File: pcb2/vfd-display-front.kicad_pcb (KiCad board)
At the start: 2 copper layers, 201.9 x 54.6 mm, 61 parts, among them CON1 AVR-ISP-10, IC1 ATMEGA88A-A, IC2 TD62C950RF, IC3 TD62C950RF, J1 HEADER_5, P1 CONN_02X05, P2 CONN_01X03, P3 CONN_01X02, P4 CONN_01X04, P5 CONN_01X02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

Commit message: Update.
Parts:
- moved CON1 0.76 mm to (116.3, 39.9)
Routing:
- net /MOSI: track 0.00 -> 41.0 mm
- net /MISO: track 0.00 -> 23.7 mm
- net /SCK: track 0.00 -> 20.1 mm
- net /SCL: track 17.9 -> 0.00 mm
- net /SDA: track 17.3 -> 0.00 mm

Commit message: Board almost done.
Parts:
- moved R13 35.2 mm to (101.1, 33.0), turned to 270 degrees
- moved Q1 35.1 mm to (101.6, 27.4)
- moved C12 25.9 mm to (178.8, 43.4), turned to 270 degrees
- moved C19 25.2 mm to (66.3, 29.0)
- moved U3 24.9 mm to (76.7, 29.5), turned to 270 degrees
- moved P6 23.7 mm to (84.6, 30.0)
- moved R14 21.4 mm to (104.9, 31.2), turned to 270 degrees
- moved C17 17.8 mm to (93.5, 29.2), turned to 180 degrees
- moved R9 16.4 mm to (56.4, 36.1), turned to 270 degrees
- moved P5 15.0 mm to (47.0, 40.9), turned to 0 degrees
- moved R8 14.1 mm to (59.4, 36.1), turned to 270 degrees
- moved C10 2.84 mm to (96.8, 47.8), turned to 180 degrees
- moved C15 2.70 mm to (51.1, 39.6), turned to 90 degrees
- moved C14 1.52 mm to (184.4, 45.2)
- moved P3 1.30 mm to (56.1, 49.5)
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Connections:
- IC1 pad 10: Net-(IC1-Pad10) -> /CHG
- IC1 pad 11: Net-(IC1-Pad11) -> /CK
- IC1 pad 12: Net-(IC1-Pad12) -> /S-IN
- IC1 pad 13: Net-(IC1-Pad13) -> /STB
- IC1 pad 14: Net-(IC1-Pad14) -> /CL
- IC1 pad 9: Net-(IC1-Pad9) -> /SPKR
- U2 pad 6: Net-(U2-Pad6) -> /BTN_WAKE
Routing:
- net +5V: track 23.4 -> 245.3 mm, vias 0 -> 4
- net /OVF: track 0.00 -> 146.0 mm, vias 0 -> 4
- net /CL: track 0.00 -> 142.6 mm, vias 0 -> 2
- net /STB: track 0.00 -> 140.7 mm, vias 0 -> 2
- net /CK: track 0.00 -> 119.5 mm, vias 0 -> 6
- net /CHG: track 0.00 -> 112.8 mm, vias 0 -> 6
- net /SDA: track 0.00 -> 110.0 mm, vias 0 -> 6
- net /SCL: track 0.00 -> 105.8 mm, vias 0 -> 2
- net /S-IN: track 0.00 -> 79.5 mm
- net GND: track 20.6 -> 93.6 mm
- net +3V3: track 0.00 -> 71.3 mm
- net Net-(P3-Pad1): track 0.00 -> 22.7 mm
- net Net-(Q1-Pad1): track 0.00 -> 19.2 mm
- net Net-(P1-Pad5): track 0.00 -> 17.4 mm
- net Net-(P1-Pad3): track 0.00 -> 17.2 mm
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
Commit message: Board beta complete.
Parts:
- moved R13 6.18 mm to (95.0, 34.0), turned to 0 degrees
- moved C10 5.08 mm to (101.9, 47.8), turned to 90 degrees
- moved C13 4.06 mm to (116.3, 29.0)
- moved C11 3.97 mm to (122.9, 29.5)
- moved C12 2.62 mm to (177.5, 41.1)
- moved C19 2.59 mm to (65.8, 31.5)
- moved L1 2.54 mm to (132.1, 30.5)
- moved C7 2.29 mm to (134.1, 53.6)
- moved C17 1.78 mm to (93.5, 27.4)
- moved P3 1.52 mm to (56.1, 48.0)
- moved P6 1.48 mm to (85.3, 28.7)
- moved U3 1.48 mm to (78.0, 28.7)
- moved R14 1.37 mm to (105.4, 30.0)
- moved R1 0.92 mm to (121.2, 38.6)
- moved C8 0.25 mm to (67.3, 45.2)
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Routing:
- net GND: track 93.6 -> 193.8 mm, vias 0 -> 4
- net /SPKR: track 0.00 -> 49.5 mm, vias 0 -> 2
- net +5V: track 245.3 -> 280.9 mm, vias 4 -> 6
- net +48V: track 154.3 -> 149.4 mm
- net Net-(C3-Pad1): track 47.0 -> 50.4 mm
- net /CK: track 119.5 -> 122.7 mm
- net /CHG: track 112.8 -> 110.0 mm
- net Net-(D7-Pad2): track 21.0 -> 18.5 mm
- net Net-(C9-Pad1): track 16.1 -> 18.4 mm
- net Net-(P2-Pad1): track 8.99 -> 11.2 mm
- net Net-(C7-Pad1): track 14.4 -> 16.5 mm
- net Net-(C3-Pad2): track 52.0 -> 54.1 mm
- net +3V3: track 71.3 -> 73.4 mm
- net Net-(Q1-Pad1): track 19.2 -> 17.4 mm
- net /SCL: track 105.8 -> 107.5 mm
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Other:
- net class Default: clearance 0.2 -> 0.3; trace_width 0.25 -> 0.4; via_dia 0.6 -> 1.2; via_drill 0.4 -> 0.8
- rule trace_clearance: 0.2 -> 0.3
- rule trace_min: 0.2 -> 0.4
- rule via_min_size: 0.4 -> 0.8
- board text added: "2016"
- board text added: "DK"
- board text added: "Michał"
- board text added: "SQ2OMC"
- board text added: "Słomkowski"
- board text added: "VFD DISP"

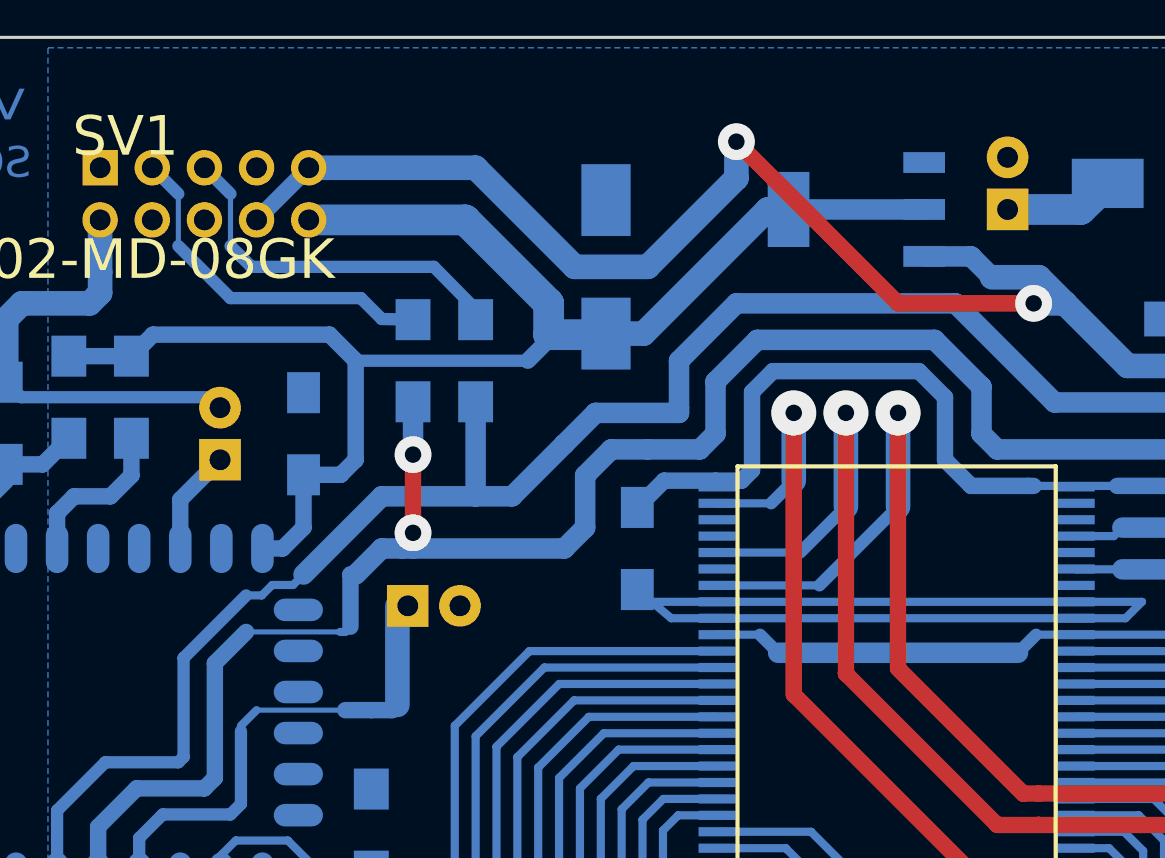
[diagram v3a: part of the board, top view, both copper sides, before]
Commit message: Make some lines thicker.
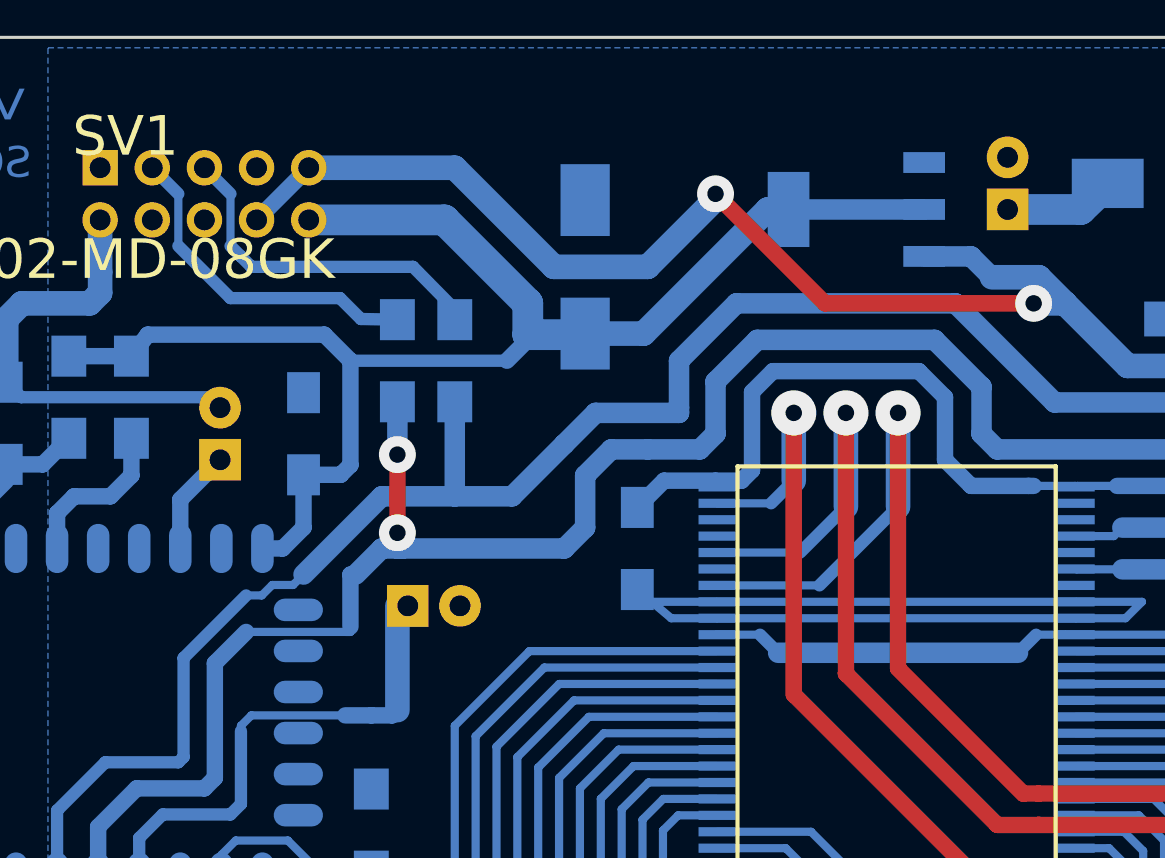
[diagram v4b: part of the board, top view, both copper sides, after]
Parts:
- moved C19 1.02 mm to (64.8, 31.5)
- moved R8 1.02 mm to (58.4, 36.1)
- moved R9 0.76 mm to (55.6, 36.1)
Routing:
- net +5V: track 280.9 -> 277.9 mm
- net +3V3: track 73.4 -> 72.3 mm
- net /SDA: track 110.2 -> 111.2 mm
- net Net-(P1-Pad5): track 17.6 -> 16.5 mm
- net Net-(P1-Pad3): track 17.2 -> 16.5 mm
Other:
- net class Default: clearance 0.3 -> 0.1
- rule pad_to_mask_clearance: 0.2 -> 0.1
- rule trace_clearance: 0.3 -> 0.1

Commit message: Add correct footprint for PCB. Fix PCB.
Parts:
- IC2, IC3: footprint futaba-vfd:futaba-vfd-SSOP60-P-0.65 -> TD62C950RF:SSOP60-P-0.65A
- R4: value 10k -> 4k7
- R5: value 10k -> 1k5
- moved C10 38.2 mm to (63.8, 50.5)
- moved C14 4.99 mm to (183.1, 50.0), turned to 90 degrees
- moved C8 4.64 mm to (68.1, 49.8)
- moved C12 4.60 mm to (177.0, 45.7), turned to 0 degrees
- moved R11 3.34 mm to (53.8, 55.6), turned to 270 degrees
- moved R3 3.10 mm to (186.9, 50.0), turned to 270 degrees
- moved IC2 2.74 mm to (166.1, 57.1)
- moved IC3 2.65 mm to (79.5, 57.1)
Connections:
- CON1 pad 3: Net-(CON1-Pad3) -> (no net)
- IC1 pad 19: Net-(IC1-Pad19) -> (no net)
- IC1 pad 2: Net-(IC1-Pad2) -> (no net)
- IC1 pad 20: Net-(IC1-Pad20) -> (no net)
- IC1 pad 22: Net-(IC1-Pad22) -> (no net)
- IC1 pad 23: Net-(IC1-Pad23) -> (no net)
- IC1 pad 24: Net-(IC1-Pad24) -> (no net)
- IC1 pad 25: Net-(IC1-Pad25) -> (no net)
- IC1 pad 26: Net-(IC1-Pad26) -> (no net)
- IC1 pad 30: Net-(IC1-Pad30) -> (no net)
- IC2 pad 1: /G34 -> (no net)
- IC2 pad 10: /G31 -> /A26
- IC2 pad 11: /G30 -> /A27
- IC2 pad 12: /G29 -> /A28
- IC2 pad 13: /G28 -> /A29
- IC2 pad 14: /G27 -> /A30
- IC2 pad 15: /G26 -> /A31
- IC2 pad 16: /G25 -> /A32
- IC2 pad 17: /G24 -> /A33
- IC2 pad 18: /G23 -> /A34
- IC2 pad 19: /G22 -> /A35
- IC2 pad 2: /G35 -> (no net)
- IC2 pad 20: /G21 -> /A36
- IC2 pad 24: /CL -> (no net)
- IC2 pad 25: (no net) -> /CHG
- IC2 pad 26: /STB -> (no net)
- IC2 pad 27: (no net) -> /CK
- IC2 pad 29: /S-IN -> /OVF
- IC2 pad 3: /G36 -> /A25
- IC2 pad 32: /OVF -> /S-IN
- IC2 pad 34: /CK -> (no net)
- IC2 pad 35: (no net) -> /STB
- IC2 pad 36: /CHG -> (no net)
- IC2 pad 37: (no net) -> /CL
- IC2 pad 4: /G37 -> /A24
- IC2 pad 41: /A36 -> /G21
- IC2 pad 42: /A35 -> /G22
- IC2 pad 43: /A34 -> /G23
- IC2 pad 44: /A33 -> /G24
- IC2 pad 45: /A32 -> /G25
- IC2 pad 46: /A31 -> /G26
- IC2 pad 47: /A30 -> /G27
- IC2 pad 48: /A29 -> /G28
- IC2 pad 49: /A28 -> /G29
- IC2 pad 5: /G38 -> /A23
- IC2 pad 50: /A27 -> /G30
- IC2 pad 51: /A26 -> /G31
- IC2 pad 52: /A19 -> /G32
- IC2 pad 53: /A20 -> /G33
- IC2 pad 54: /A21 -> /G40
- IC2 pad 55: /A22 -> /G39
- IC2 pad 56: /A23 -> /G38
- IC2 pad 57: /A24 -> /G37
- IC2 pad 58: /A25 -> /G36
- IC2 pad 59: Net-(IC2-Pad59) -> /G35
- IC2 pad 6: /G39 -> /A22
- IC2 pad 60: Net-(IC2-Pad60) -> /G34
- IC2 pad 7: /G40 -> /A21
- IC2 pad 8: /G33 -> /A20
- IC2 pad 9: /G32 -> /A19
- IC3 pad 1: /A13 -> /G7
- IC3 pad 10: /A11 -> /G10
- IC3 pad 11: /A10 -> /G11
- IC3 pad 12: /A9 -> /G12
- IC3 pad 13: /A8 -> /G13
- IC3 pad 14: /A7 -> /G14
- IC3 pad 15: /A6 -> /G15
- IC3 pad 16: /A5 -> /G16
- IC3 pad 17: /A4 -> /G17
- IC3 pad 18: /A3 -> /G18
- IC3 pad 19: /A2 -> /G19
- IC3 pad 2: /A12 -> /G6
- IC3 pad 20: /A1 -> /G20
- IC3 pad 24: /CL -> (no net)
- IC3 pad 25: (no net) -> /CHG
- IC3 pad 26: /STB -> (no net)
- IC3 pad 27: (no net) -> /CK
- IC3 pad 29: /OVF -> (no net)
- IC3 pad 3: Net-(IC3-Pad3) -> /G5
- IC3 pad 32: Net-(IC3-Pad32) -> /OVF
- IC3 pad 34: /CK -> (no net)
- IC3 pad 35: (no net) -> /STB
- IC3 pad 36: /CHG -> (no net)
- IC3 pad 37: (no net) -> /CL
- IC3 pad 4: Net-(IC3-Pad4) -> /G4
- IC3 pad 41: /G20 -> /A1
- IC3 pad 42: /G19 -> /A2
- IC3 pad 43: /G18 -> /A3
- IC3 pad 44: /G17 -> /A4
- IC3 pad 45: /G16 -> /A5
- IC3 pad 46: /G15 -> /A6
- IC3 pad 47: /G14 -> /A7
- IC3 pad 48: /G13 -> /A8
- IC3 pad 49: /G12 -> /A9
- IC3 pad 5: /A14 -> /G3
- IC3 pad 50: /G11 -> /A10
- IC3 pad 51: /G10 -> /A11
- IC3 pad 52: /G9 -> /A18
- IC3 pad 53: /G8 -> /A17
- IC3 pad 54: /G1 -> /A16
- IC3 pad 55: /G2 -> /A15
- IC3 pad 56: /G3 -> /A14
- IC3 pad 57: /G4 -> (no net)
- IC3 pad 58: /G5 -> (no net)
- IC3 pad 59: /G6 -> /A12
- IC3 pad 6: /A15 -> /G2
- IC3 pad 60: /G7 -> /A13
- IC3 pad 7: /A16 -> /G1
- IC3 pad 8: /A17 -> /G8
- IC3 pad 9: /A18 -> /G9
- P1 pad 4: Net-(P1-Pad4) -> (no net)
- P1 pad 6: Net-(P1-Pad6) -> (no net)
- P1 pad 7: Net-(P1-Pad7) -> (no net)
- U2 pad 10: Net-(U2-Pad10) -> (no net)
- U2 pad 11: Net-(U2-Pad11) -> (no net)
- U2 pad 12: Net-(U2-Pad12) -> (no net)
- U2 pad 13: Net-(U2-Pad13) -> (no net)
- U2 pad 14: Net-(U2-Pad14) -> (no net)
- U2 pad 17: Net-(U2-Pad17) -> (no net)
- U2 pad 2: Net-(U2-Pad2) -> (no net)
- U2 pad 4: Net-(U2-Pad4) -> (no net)
- U2 pad 5: Net-(U2-Pad5) -> (no net)
- U2 pad 7: Net-(U2-Pad7) -> (no net)
- U2 pad 9: Net-(U2-Pad9) -> (no net)
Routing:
- net GND: track 193.8 -> 253.9 mm
- net +48V: track 149.4 -> 176.5 mm
- net /STB: track 140.9 -> 127.5 mm
- net /CL: track 142.6 -> 129.5 mm
- net +5V: track 277.9 -> 288.7 mm
- net /OVF: track 145.2 -> 134.4 mm
- net /S-IN: track 78.2 -> 69.9 mm
- net Net-(R11-Pad1): track 9.29 -> 14.6 mm
- net /SDA: track 111.2 -> 106.3 mm
- net /CHG: track 110.0 -> 113.6 mm
- net /SCL: track 107.5 -> 104.0 mm
- net Net-(R2-Pad1): track 8.80 -> 5.52 mm
- net Net-(P3-Pad1): track 24.4 -> 21.3 mm
- net /A2: track 32.4 -> 29.8 mm
- net /A1: track 34.3 -> 31.8 mm
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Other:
- net class VFD Sig removed
- board text added: "AB"
- board text added: "FoE"
- board text removed: "DK"
